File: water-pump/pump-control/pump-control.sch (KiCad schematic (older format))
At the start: 18 parts, among them J1 pressure contact, J2 SSR control, J3 Display, J4 Temperature sensors, J5 230V AC, J6 Manual reset, J7 Temperature sensors, SW1 Manual reset, U1 ATmega328P-PU, U2 NRF24L01_Breakout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

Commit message: Schema + PCB
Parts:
- added C4: 100u, Capacitor_THT:CP_Radial_D7.5mm_P2.50mm, symbol Device:CP
- added C5: .1u, Capacitor_THT:C_Rect_L18.0mm_W6.0mm_P15.00mm_FKS3_FKP3, symbol Device:C_Small
- added D1: LED_btn, Connector_PinHeader_2.54mm:PinHeader_1x02_P2.54mm_Vertical, symbol Device:LED_Small
- added H1, H2: MountingHole, MountingHole:MountingHole_3.2mm_M3, symbol Mechanical:MountingHole
- added L1: 10mH, Inductor_THT:L_CommonMode_Toroid_Vertical_L21.0mm_W10.0mm_Px5.08mm_Py12.70mm_muRATA_5100, symbol Device:L_Core_Ferrite_Coupled_Small_1423
- added R3: 330, Resistor_THT:R_Axial_DIN0207_L6.3mm_D2.5mm_P10.16mm_Horizontal, symbol Device:R
- added RV1: 300/450V, Varistor:RV_Disc_D12mm_W3.9mm_P7.5mm, symbol Device:Varistor
- F1: value Fuse_Small -> .5A
- J1, J2: footprint Connector_AMASS:AMASS_XT30UPB-M_1x02_P5.0mm_Vertical -> TerminalBlock_Phoenix:TerminalBlock_Phoenix_MKDS-1,5-2-5.08_1x02_P5.08mm_Horizontal
- J5: footprint Connector_PinSocket_2.54mm:PinSocket_1x02_P2.54mm_Vertical -> TerminalBlock_Phoenix:TerminalBlock_Phoenix_MKDS-1,5-3-5.08_1x03_P5.08mm_Horizontal; symbol Connector:Screw_Terminal_01x02 -> Connector:Screw_Terminal_01x03
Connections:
- net labels added: L, N
- wire segments 88 -> 107
- no-connect marks 13 -> 12
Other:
- moved on the sheet: F1
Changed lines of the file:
@@
 F 0 "J1" H 7530 3892 50  0000 L CNN
 F 1 "pressure contact" H 7530 3801 50  0000 L CNN
-F 2 "Connector_AMASS:AMASS_XT30UPB-M_1x02_P5.0mm_Vertical" H 7450 3900 50  0001 C CNN
+F 2 "TerminalBlock_Phoenix:TerminalBlock_Phoenix_MKDS-1,5-2-5.08_1x02_P5.08mm_Horizontal" H 7450 3900 50  0001 C CNN
 F 3 "~" H 7450 3900 50  0001 C CNN
 	1    7450 3900
@@
 F 0 "J2" H 7530 4142 50  0000 L CNN
 F 1 "SSR control" H 7530 4051 50  0000 L CNN
-F 2 "Connector_AMASS:AMASS_XT30UPB-M_1x02_P5.0mm_Vertical" H 7450 4150 50  0001 C CNN
+F 2 "TerminalBlock_Phoenix:TerminalBlock_Phoenix_MKDS-1,5-2-5.08_1x02_P5.08mm_Horizontal" H 7450 4150 50  0001 C CNN
 F 3 "~" H 7450 4150 50  0001 C CNN
 	1    7450 4150
@@
 NoConn ~ 6100 3600
 NoConn ~ 6100 3700
-NoConn ~ 6100 4200
 NoConn ~ 6100 4300
 Text Label 6950 1350 0    50   ~ 0
@@
 L power:PWR_FLAG #FLG0101
 U 1 1 5FA8045E
-P 3500 800
-F 0 "#FLG0101" H 3500 875 50  0001 C CNN
-F 1 "PWR_FLAG" H 3500 973 50  0000 C CNN
-F 2 "" H 3500 800 50  0001 C CNN
-F 3 "~" H 3500 800 50  0001 C CNN
-	1    3500 800
-	1    0    0    -1
+P 4000 1300
+F 0 "#FLG0101" H 4000 1375 50  0001 C CNN
+F 1 "PWR_FLAG" H 4000 1473 50  0000 C CNN
+F 2 "" H 4000 1300 50  0001 C CNN
+F 3 "~" H 4000 1300 50  0001 C CNN
+	1    4000 1300
+	-1   0    0    1
 $EndComp
 $Comp
 L power:PWR_FLAG #FLG0102
 U 1 1 5FA8139A
-P 3750 800
-F 0 "#FLG0102" H 3750 875 50  0001 C CNN
-F 1 "PWR_FLAG" H 3750 973 50  0000 C CNN
-F 2 "" H 3750 800 50  0001 C CNN
-F 3 "~" H 3750 800 50  0001 C CNN
-	1    3750 800
+P 4000 750
+F 0 "#FLG0102" H 4000 825 50  0001 C CNN
+F 1 "PWR_FLAG" H 4000 923 50  0000 C CNN
+F 2 "" H 4000 750 50  0001 C CNN
+F 3 "~" H 4000 750 50  0001 C CNN
+	1    4000 750
 	1    0    0    -1
 $EndComp
@@
 $EndComp
 Wire Wire Line
-	6200 1000 5500 1000
+	6200 1000 5900 1000
 Connection ~ 5500 1000
 Wire Wire Line
@@
 	6250 3800 6500 3800
 Wire Wire Line
-	5500 5100 7150 5100
+	5500 5100 6200 5100
 Wire Wire Line
 	6900 3800 7150 3800
@@
 	4950 1500 5200 1500
 $Comp
-L Connector:Screw_Terminal_01x02 J5
+L Connector:Screw_Terminal_01x03 J5
 U 1 1 5FA71ED4
-P 2750 1050
-F 0 "J5" H 2830 1042 50  0000 L CNN
-F 1 "230V AC" H 2830 951 50  0000 L CNN
-F 2 "Connector_PinSocket_2.54mm:PinSocket_1x02_P2.54mm_Vertical" H 2750 1050 50  0001 C CNN
-F 3 "~" H 2750 1050 50  0001 C CNN
-	1    2750 1050
-	-1   0    0    1
+P 2650 1050
+F 0 "J5" H 2730 1042 50  0000 L CNN
+F 1 "230V AC" H 2730 951 50  0000 L CNN
+F 2 "TerminalBlock_Phoenix:TerminalBlock_Phoenix_MKDS-1,5-3-5.08_1x03_P5.08mm_Horizontal" H 2650 1050 50  0001 C CNN
+F 3 "~" H 2650 1050 50  0001 C CNN
+	1    2650 1050
+	-1   0    0    -1
 $EndComp
 $Comp
 L Device:Fuse_Small F1
 U 1 1 5FA73702
-P 3200 900
-F 0 "F1" H 3200 1085 50  0000 C CNN
-F 1 "Fuse_Small" H 3200 994 50  0000 C CNN
-F 2 "Fuse:Fuseholder_TR5_Littelfuse_No560_No460" H 3200 993 50  0001 C CNN
-F 3 "~" H 3200 900 50  0001 C CNN
-	1    3200 900
-	1    0    0    -1
-$EndComp
-Wire Wire Line
-	2950 950  3100 950
-Wire Wire Line
-	3300 900  3750 900
-Wire Wire Line
-	2950 1050 3500 1050
-Wire Wire Line
-	4050 1050 4050 1100
-Wire Wire Line
-	3100 950  3100 900
-Wire Wire Line
-	3500 800  3500 1050
-Connection ~ 3500 1050
-Wire Wire Line
-	3500 1050 4050 1050
-Wire Wire Line
-	3750 800  3750 900
-Connection ~ 3750 900
-Wire Wire Line
-	3750 900  4050 900
+P 3050 850
+F 0 "F1" H 3050 1035 50  0000 C CNN
+F 1 ".5A" H 3050 944 50  0000 C CNN
+F 2 "Fuse:Fuseholder_TR5_Littelfuse_No560_No460" H 3050 943 50  0001 C CNN
+F 3 "~" H 3050 850 50  0001 C CNN
+	1    3050 850
+	1    0    0    -1
+$EndComp
 Wire Wire Line
 	6650 2850 6650 3400
@@
 Wire Wire Line
 	6900 4500 7400 4500
+$Comp
+L Device:CP C4
+U 1 1 5FB0BA90
+P 5900 1150
+F 0 "C4" H 6018 1196 50  0000 L CNN
+F 1 "100u" H 6018 1105 50  0000 L CNN
+F 2 "Capacitor_THT:CP_Radial_D7.5mm_P2.50mm" H 5938 1000 50  0001 C CNN
+F 3 "~" H 5900 1150 50  0001 C CNN
+	1    5900 1150
+	1    0    0    -1
+$EndComp
+Connection ~ 5900 1000
+Wire Wire Line
+	5900 1000 5500 1000
+Wire Wire Line
+	5900 1300 6500 1300
+Connection ~ 6500 1300
+$Comp
+L Device:C_Small C5
+U 1 1 5FB1C8B8
+P 3550 1000
+F 0 "C5" H 3500 1250 50  0000 L CNN
+F 1 ".1u" H 3550 800 50  0000 L CNN
+F 2 "Capacitor_THT:C_Rect_L18.0mm_W6.0mm_P15.00mm_FKS3_FKP3" H 3550 1000 50  0001 C CNN
+F 3 "~" H 3550 1000 50  0001 C CNN
+	1    3550 1000
+	1    0    0    -1
+$EndComp
+$Comp
+L Device:Varistor RV1
+U 1 1 5FB251E3
+P 3300 1000
+F 0 "RV1" H 3250 1250 50  0000 L CNN
+F 1 "300/450V" H 3100 800 50  0000 L CNN
+F 2 "Varistor:RV_Disc_D12mm_W3.9mm_P7.5mm" V 3230 1000 50  0001 C CNN
+F 3 "~" H 3300 1000 50  0001 C CNN
+	1    3300 1000
+	1    0    0    -1
+$EndComp
+Wire Wire Line
+	3950 950  4000 950
+Wire Wire Line
+	4050 950  4050 900
+Wire Wire Line
+	3950 1050 4000 1050
+Wire Wire Line
+	4050 1050 4050 1100
+Wire Wire Line
+	3550 900  3750 900
+Wire Wire Line
+	3750 900  3750 950
+Wire Wire Line
+	3550 1100 3750 1100
+Wire Wire Line
+	3750 1100 3750 1050
+Wire Wire Line
+	3300 1150 3550 1150
+Wire Wire Line
+	3550 1150 3550 1100
+Connection ~ 3550 1100
+Wire Wire Line
+	3300 850  3550 850
+Wire Wire Line
+	3550 850  3550 900
+Connection ~ 3550 900
+Wire Wire Line
+	3150 850  3300 850
+Connection ~ 3300 850
+Wire Wire Line
+	2850 850  2850 950
+Connection ~ 3300 1150
+Wire Wire Line
+	2850 1150 2850 1050
+Connection ~ 2850 1150
+Text Label 2800 950  0    50   ~ 0
+L
+Text Label 2800 1050 0    50   ~ 0
+N
+Text Label 2800 1150 0    50   ~ 0
+N
+Wire Wire Line
+	2850 1150 3300 1150
+Wire Wire Line
+	4000 750  4000 950
+Connection ~ 4000 950
+Wire Wire Line
+	4000 950  4050 950
+Wire Wire Line
+	4000 1300 4000 1050
+Connection ~ 4000 1050
+Wire Wire Line
+	4000 1050 4050 1050
+Wire Wire Line
+	2850 850  2950 850
+$Comp
+L Device:L_Core_Ferrite_Coupled_Small_1423 L1
+U 1 1 5FB1D4B8
+P 3850 1000
+F 0 "L1" H 3850 1231 50  0000 C CNN
+F 1 "10mH" H 3850 1140 50  0000 C CNN
+F 2 "Inductor_THT:L_CommonMode_Toroid_Vertical_L21.0mm_W10.0mm_Px5.08mm_Py12.70mm_muRATA_5100" H 3850 1000 50  0001 C CNN
+F 3 "~" H 3850 1000 50  0001 C CNN
+	1    3850 1000
+	1    0    0    -1
+$EndComp
+$Comp
+L Device:R R3
+U 1 1 5FB3C1A1
+P 6200 4600
+F 0 "R3" H 6270 4646 50  0000 L CNN
+F 1 "330" H 6270 4555 50  0000 L CNN
+F 2 "Resistor_THT:R_Axial_DIN0207_L6.3mm_D2.5mm_P10.16mm_Horizontal" V 6130 4600 50  0001 C CNN
+F 3 "~" H 6200 4600 50  0001 C CNN
+	1    6200 4600
+	1    0    0    -1
+$EndComp
+Wire Wire Line
+	6100 4200 6200 4200
+Wire Wire Line
+	6200 4200 6200 4450
+$Comp
+L Device:LED_Small D1
+U 1 1 5FB40DAC
+P 6200 4900
+F 0 "D1" V 6246 4830 50  0000 R CNN
+F 1 "LED_btn" V 6155 4830 50  0000 R CNN
+F 2 "Connector_PinHeader_2.54mm:PinHeader_1x02_P2.54mm_Vertical" V 6200 4900 50  0001 C CNN
+F 3 "~" V 6200 4900 50  0001 C CNN
+	1    6200 4900
+	0    -1   -1   0
+$EndComp
+Wire Wire Line
+	6200 4750 6200 4800
+Wire Wire Line
+	6200 5000 6200 5100
+Connection ~ 6200 5100
+Wire Wire Line
+	6200 5100 7150 5100
+$Comp
+L Mechanical:MountingHole H1
+U 1 1 5FB501F7
+P 3350 1950
+F 0 "H1" H 3450 1996 50  0000 L CNN
+F 1 "MountingHole" H 3450 1905 50  0000 L CNN
+F 2 "MountingHole:MountingHole_3.2mm_M3" H 3350 1950 50  0001 C CNN
+F 3 "~" H 3350 1950 50  0001 C CNN
+	1    3350 1950
+	1    0    0    -1
+$EndComp
+$Comp
+L Mechanical:MountingHole H2
+U 1 1 5FB50764
+P 3350 2250
+F 0 "H2" H 3450 2296 50  0000 L CNN
+F 1 "MountingHole" H 3450 2205 50  0000 L CNN
+F 2 "MountingHole:MountingHole_3.2mm_M3" H 3350 2250 50  0001 C CNN
+F 3 "~" H 3350 2250 50  0001 C CNN
+	1    3350 2250
+	1    0    0    -1
+$EndComp
 $EndSCHEMATC

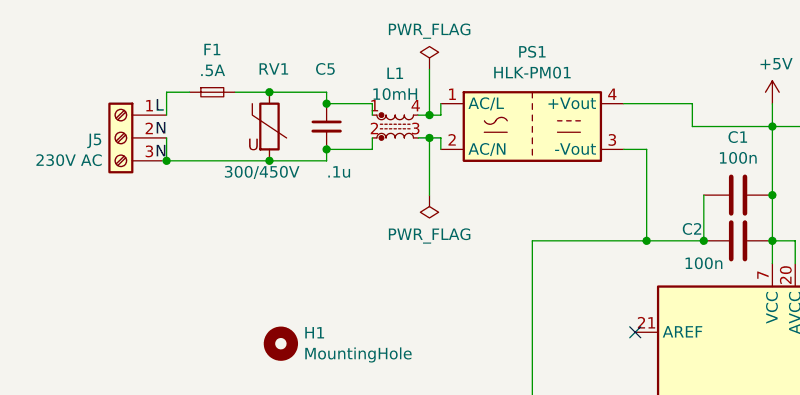
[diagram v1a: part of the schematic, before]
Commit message: Fixed input inductor pinout
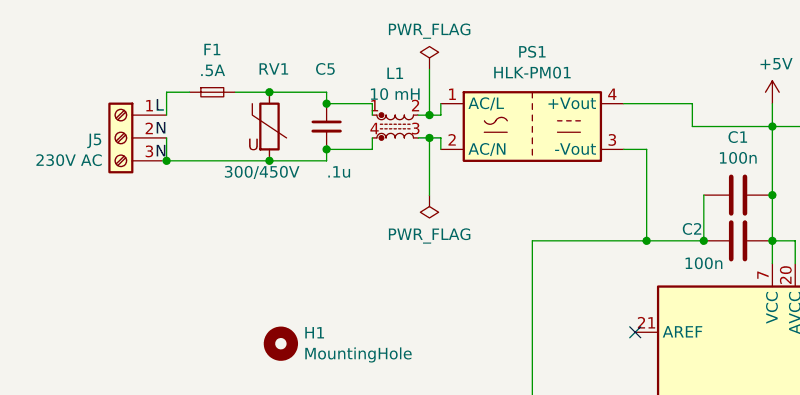
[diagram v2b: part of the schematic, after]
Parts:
- removed L1: 10mH, Inductor_THT:L_CommonMode_Toroid_Vertical_L21.0mm_W10.0mm_Px5.08mm_Py12.70mm_muRATA_5100, symbol Device:L_Core_Ferrite_Coupled_Small_1423
- added L1: 10 mH, Inductor_THT:L_CommonMode_Wuerth_WE-CMB-XS, symbol Device:L_Core_Ferrite_Coupled_Small_1243
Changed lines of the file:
@@
 	2850 850  2950 850
-$Comp
-L Device:L_Core_Ferrite_Coupled_Small_1423 L1
-U 1 1 5FB1D4B8
-P 3850 1000
-F 0 "L1" H 3850 1231 50  0000 C CNN
-F 1 "10mH" H 3850 1140 50  0000 C CNN
-F 2 "Inductor_THT:L_CommonMode_Toroid_Vertical_L21.0mm_W10.0mm_Px5.08mm_Py12.70mm_muRATA_5100" H 3850 1000 50  0001 C CNN
-F 3 "~" H 3850 1000 50  0001 C CNN
-	1    3850 1000
-	1    0    0    -1
-$EndComp
 $Comp
 L Device:R R3
@@
 	1    0    0    -1
 $EndComp
+$Comp
+L Device:L_Core_Ferrite_Coupled_Small_1243 L1
+U 1 1 5FE66F9A
+P 3850 1000
+F 0 "L1" H 3850 1231 50  0000 C CNN
+F 1 "10 mH" H 3850 1140 50  0000 C CNN
+F 2 "Inductor_THT:L_CommonMode_Wuerth_WE-CMB-XS" H 3850 1000 50  0001 C CNN
+F 3 "~" H 3850 1000 50  0001 C CNN
+	1    3850 1000
+	1    0    0    -1
+$EndComp
